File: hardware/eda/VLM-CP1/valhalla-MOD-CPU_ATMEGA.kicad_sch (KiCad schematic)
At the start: 16 parts, among them J1 ICSP, J2 BUS, U1 ATmega328PB-A, Y1 7.3728 MHz

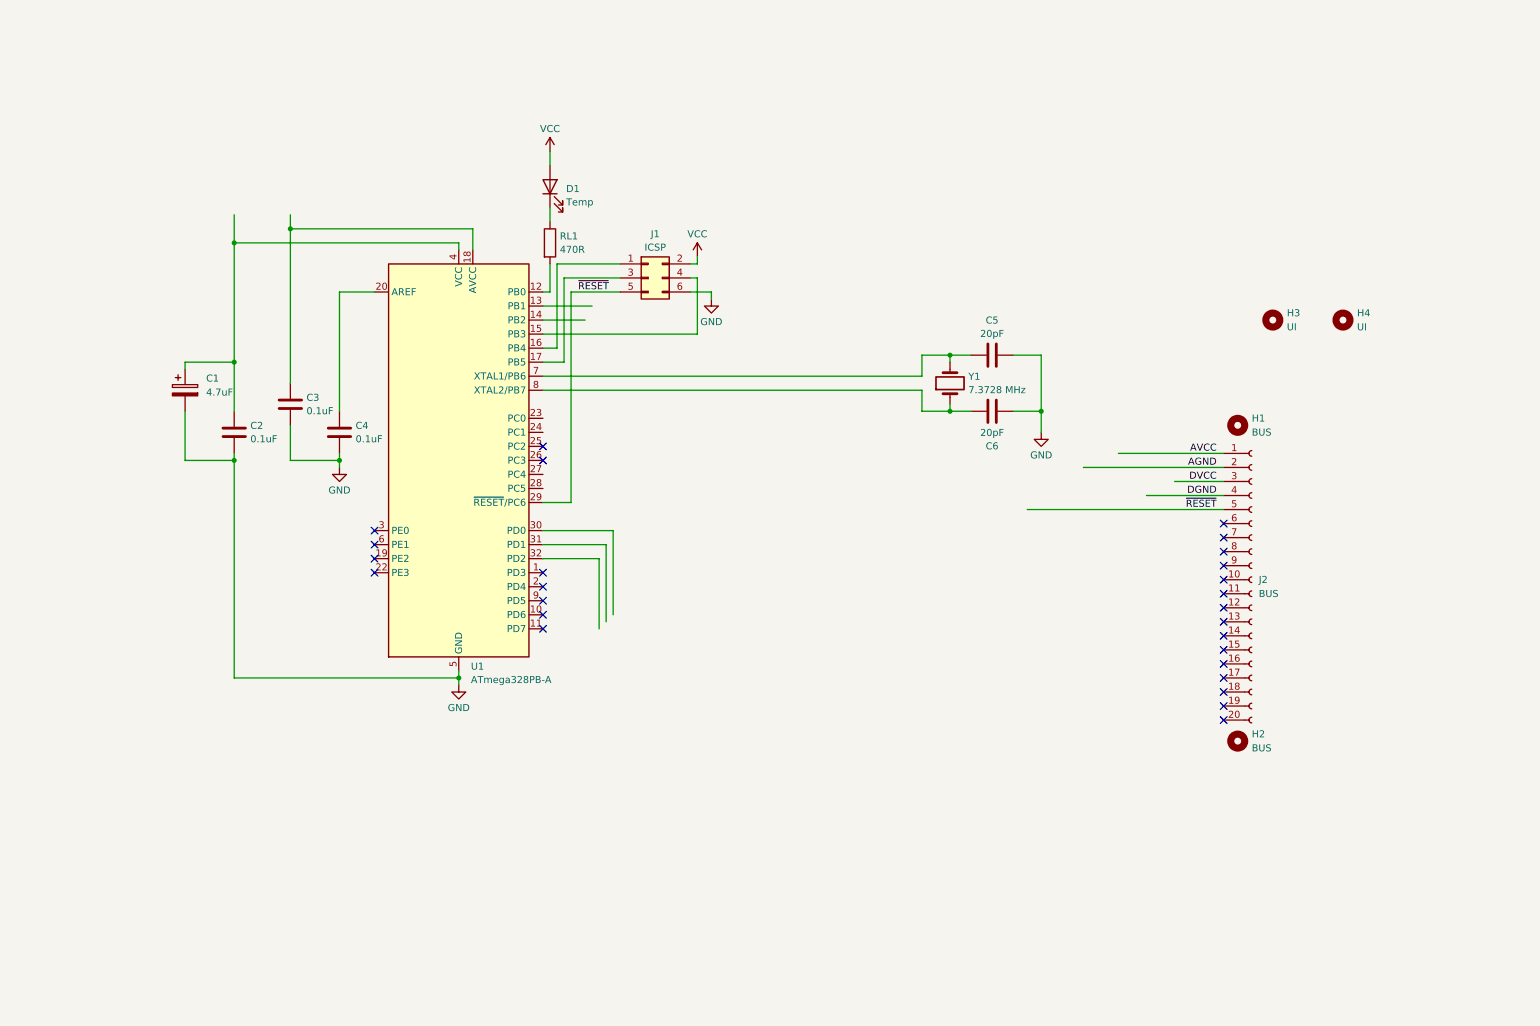
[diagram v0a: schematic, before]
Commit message: UPDATE: progress with the CPU(ATMega328) module
 - ATMega328 boilerplate done, BUS and UI done, GPIO done
 - LED UI in progress.
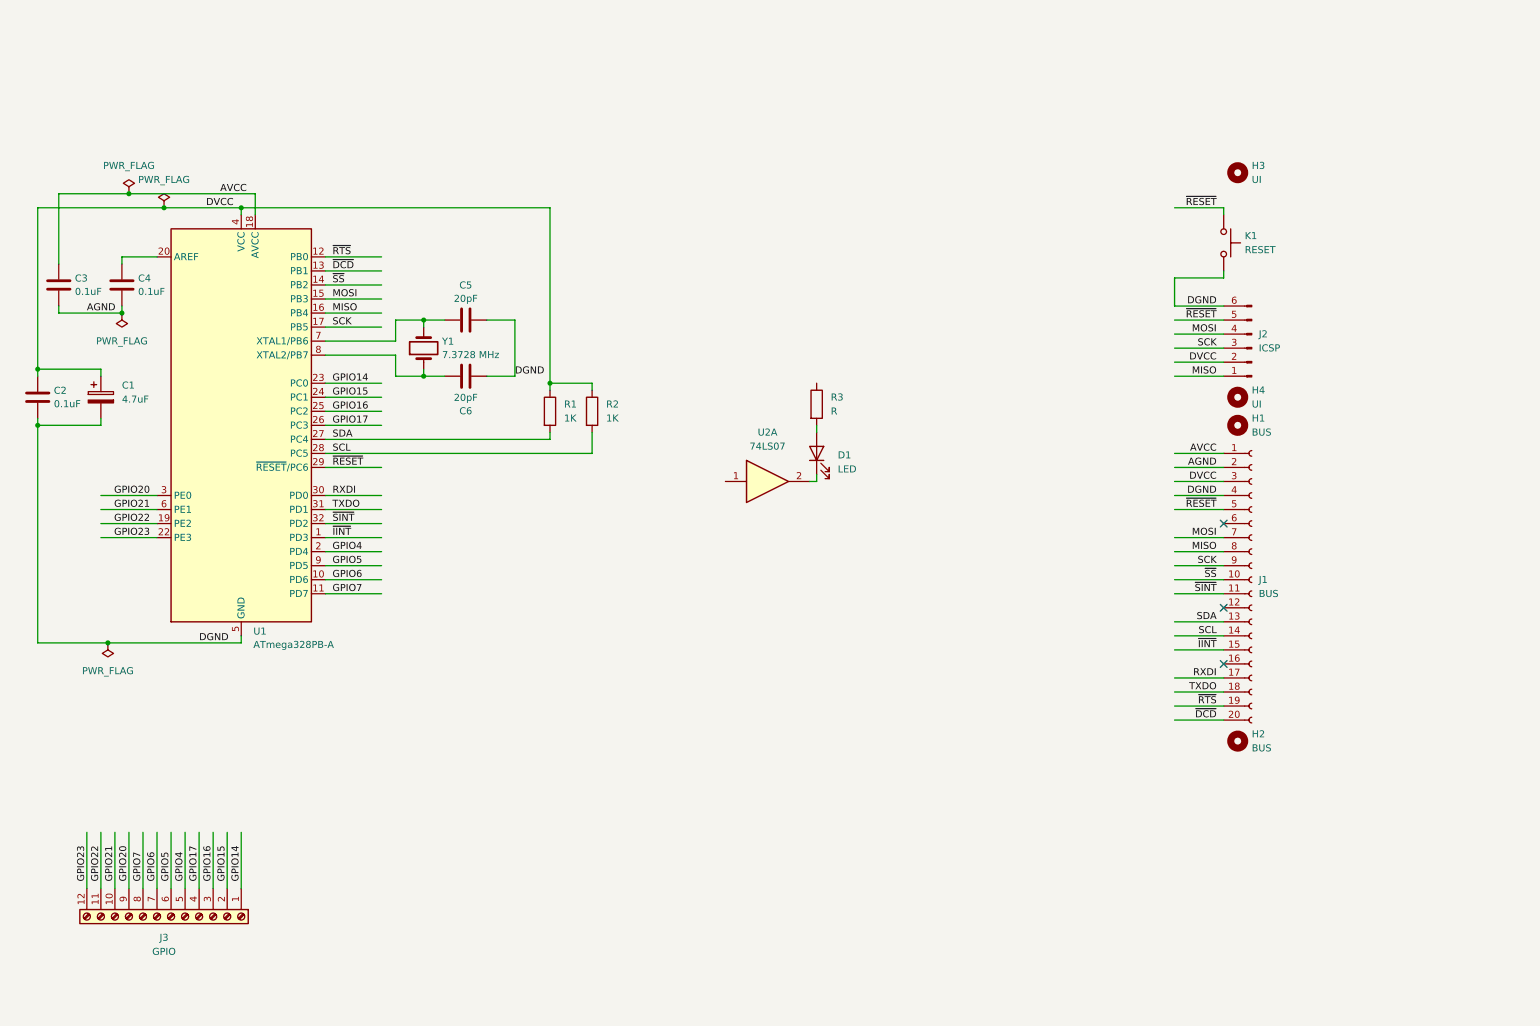
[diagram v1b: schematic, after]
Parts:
- removed J1: ICSP, Connector_IDC:IDC-Header_2x03_P2.54mm_Vertical, symbol Connector_Generic:Conn_02x03_Odd_Even
- removed RL1: 470R, Resistor_SMD:R_1206_3216Metric, symbol Device:R
- added J2: ICSP, Connector_IDC:IDC-Header_2x03_P2.54mm_Horizontal, symbol Connector:Conn_01x06_Pin
- added J3: GPIO, symbol Connector:Screw_Terminal_01x12
- added K1: RESET, symbol Switch:SW_Push
- added R1, R2: 1K, symbol Device:R
- added R3: R, symbol Device:R
- added U2: 74LS07, symbol 74xx:74LS07
- D1: value Temp -> LED; footprint LED_THT:LED_D5.0mm -> LED_THT:LED_D3.0mm_Horizontal_O1.27mm_Z2.0mm
- renumbered J2 to J1
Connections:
- net AGND: now also C3.2, C4.2
- net AVCC: now also C3.1, U1.18 (AVCC)
- net DGND: now also C1.2, C2.2, C5.2, C6.2, U1.21 (GND), U1.5 (GND), J2.6 (Pin_6), K1.2
- net DVCC: now also C1.1, C2.1, U1.4 (VCC), J2.2 (Pin_2), R1.1, R2.1
- net ~{RESET}: now also J2.5 (Pin_5), K1.1
- net at D1.1 (K): now also U2.2
- net ~{RTS}: now reaches U1.12 (PB0)
- net ~{RTS}: now also J1.19 (Pin_19)
- net MISO: now reaches U1.16 (PB4)
- net MISO: now also J1.8 (Pin_8), J2.1 (Pin_1)
- net SCK: now reaches U1.17 (PB5)
- net SCK: now also J1.9 (Pin_9), J2.3 (Pin_3)
- net MOSI: now reaches U1.15 (PB3)
- net MOSI: now also J1.7 (Pin_7), J2.4 (Pin_4)
- net ~{SS}: now reaches J1.10 (Pin_10)
- net ~{SS}: now also U1.14 (PB2)
- net ~{SINT}: now reaches J1.11 (Pin_11)
- net ~{SINT}: now also U1.32 (PD2)
- net SDA: now reaches J1.13 (Pin_13)
- net SDA: now also U1.27 (PC4), R1.2
- net SCL: now reaches J1.14 (Pin_14)
- net SCL: now also U1.28 (PC5), R2.2
- net ~{IINT}: now reaches J1.15 (Pin_15)
- net ~{IINT}: now also U1.1 (PD3)
- net RXDI: now reaches J1.17 (Pin_17)
- net RXDI: now also U1.30 (PD0)
- net TXDO: now reaches J1.18 (Pin_18)
- net TXDO: now also U1.31 (PD1)
- net ~{DCD}: now reaches J1.20 (Pin_20)
- net ~{DCD}: now also U1.13 (PB1)
- net GPIO6: now reaches U1.10 (PD6)
- net GPIO6: now also J3.7 (Pin_7)
- net GPIO7: now reaches U1.11 (PD7)
- net GPIO7: now also J3.8 (Pin_8)
- net GPIO22: now reaches U1.19 (PE2)
- net GPIO22: now also J3.11 (Pin_11)
- net GPIO4: now reaches U1.2 (PD4)
- net GPIO4: now also J3.5 (Pin_5)
- net GPIO23: now reaches U1.22 (PE3)
- net GPIO23: now also J3.12 (Pin_12)
- net GPIO14: now reaches U1.23 (PC0)
- net GPIO14: now also J3.1 (Pin_1)
- net GPIO15: now reaches U1.24 (PC1)
- net GPIO15: now also J3.2 (Pin_2)
- net GPIO16: now reaches U1.25 (PC2)
- net GPIO16: now also J3.3 (Pin_3)
- net GPIO17: now reaches U1.26 (PC3)
- net GPIO17: now also J3.4 (Pin_4)
- net GPIO20: now reaches U1.3 (PE0)
- net GPIO20: now also J3.9 (Pin_9)
- net GPIO21: now reaches U1.6 (PE1)
- net GPIO21: now also J3.10 (Pin_10)
- net GPIO5: now reaches U1.9 (PD5)
- net GPIO5: now also J3.6 (Pin_6)
- removed net GND: C1.2, C2.2, C3.2, C4.2, C5.2, C6.2, U1.21 (GND), U1.5 (GND)
- net VCC: no longer names the net of D1.2 (A)
- net VCC: now also R3.2
- no-connect marks 26 -> 3
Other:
- moved on the sheet: C1, C2, C3, C4, C5, C6, H3, H4, U1, Y1

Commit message: UPDATE: schematic complete of Valhalla-MOD CPU (ATMega) module
  - we still don't have a solution for powering the LEDs while obeying
    the design constraint that all modules must be agnostic to Vio
    inside [3.3V, 5V]
  - initial PCB component placement hints at 3" height for CPU (ATMega)
    module.
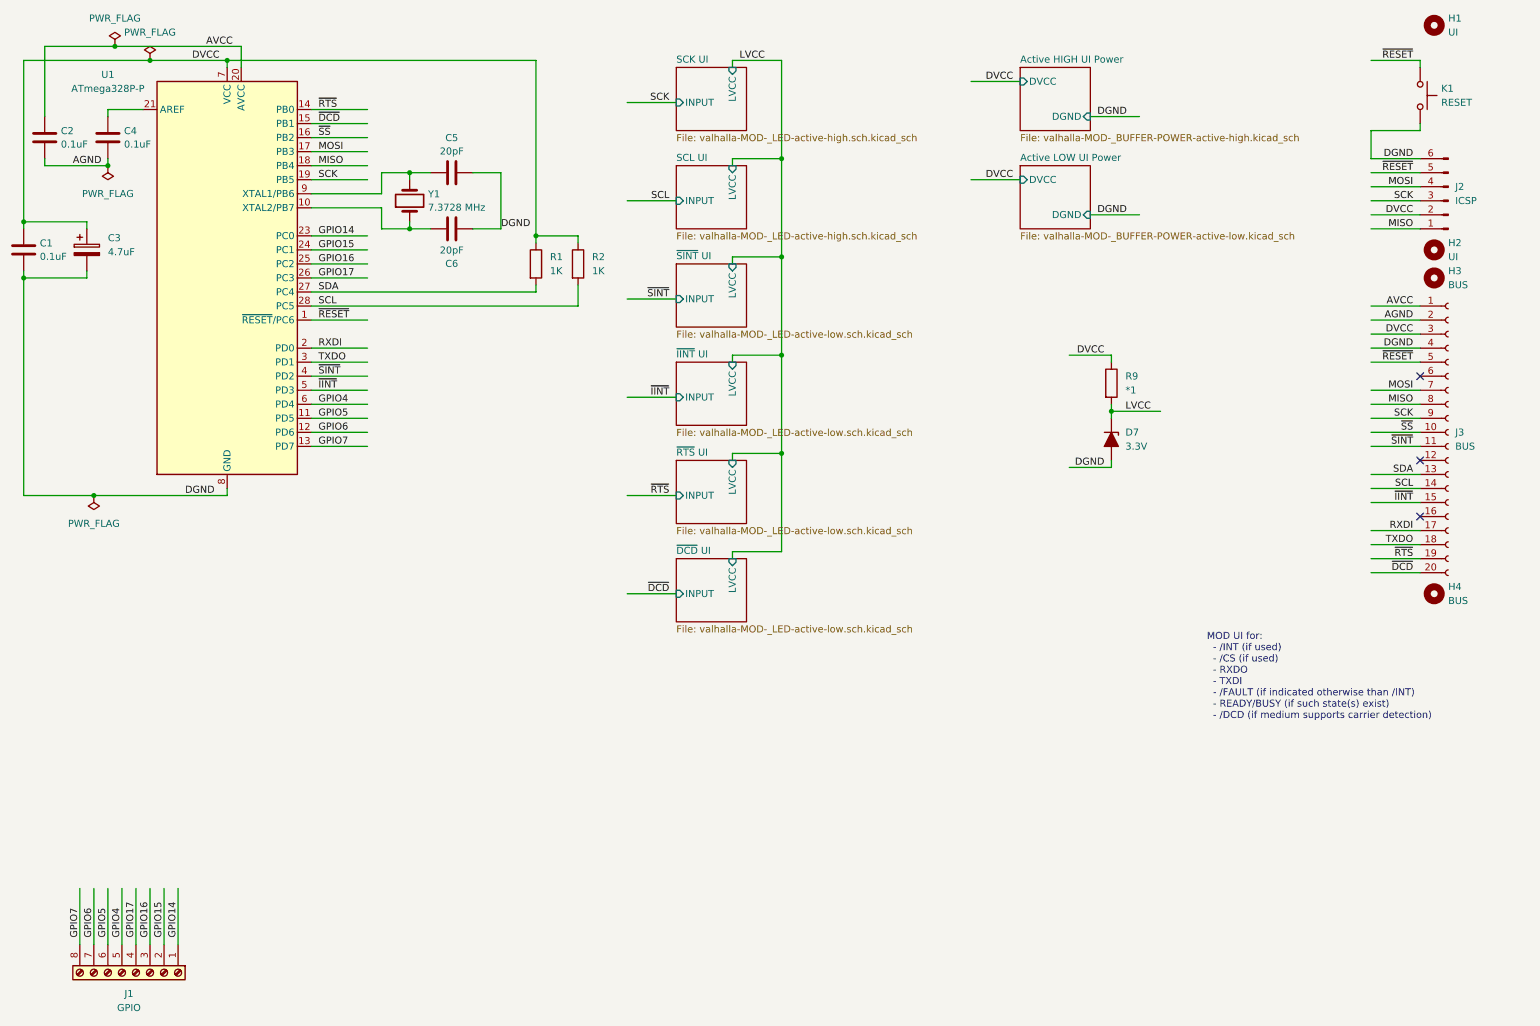
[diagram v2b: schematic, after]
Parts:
- removed D1: LED, LED_THT:LED_D3.0mm_Horizontal_O1.27mm_Z2.0mm, symbol Device:LED
- removed J3: GPIO, symbol Connector:Screw_Terminal_01x12
- removed R3: R, symbol Device:R
- removed U1: ATmega328PB-A, Package_QFP:TQFP-32_7x7mm_P0.8mm, symbol MCU_Microchip_ATmega:ATmega328PB-A
- removed U2: 74LS07, symbol 74xx:74LS07
- added D7: 3.3V, Diode_THT:D_DO-35_SOD27_P7.62mm_Horizontal, symbol Device:D_Zener_Filled
- added J1: GPIO, TerminalBlock_Phoenix:TerminalBlock_Phoenix_MPT-0,5-8-2.54_1x08_P2.54mm_Horizontal, symbol Connector:Screw_Terminal_01x08
- added R9: *1, Resistor_THT:R_Axial_DIN0309_L9.0mm_D3.2mm_P12.70mm_Horizontal, symbol Device:R
- added U1: ATmega328P-P, Package_DIP:DIP-28_W7.62mm, symbol MCU_Microchip_ATmega:ATmega328P-P
- C1: renamed from C2; footprint Capacitor_SMD:C_1206_3216Metric -> Capacitor_THT:C_Rect_L4.6mm_W2.0mm_P2.50mm_MKS02_FKP02
- C2: renamed from C3; footprint Capacitor_SMD:C_1206_3216Metric -> Capacitor_THT:C_Rect_L4.6mm_W2.0mm_P2.50mm_MKS02_FKP02
- C3: renamed from C1; footprint Capacitor_SMD:C_1206_3216Metric -> Capacitor_THT:CP_Radial_D5.0mm_P2.50mm
- C4: footprint Capacitor_SMD:C_1206_3216Metric -> Capacitor_THT:C_Rect_L4.6mm_W2.0mm_P2.50mm_MKS02_FKP02
- C5, C6: footprint Capacitor_SMD:C_1206_3216Metric -> Capacitor_THT:C_Disc_D5.0mm_W2.5mm_P5.00mm
- K1: footprint (none) -> Button_Switch_THT:SW_Tactile_SKHH_Angled
- R1, R2: footprint (none) -> Resistor_THT:R_Axial_DIN0309_L9.0mm_D3.2mm_P12.70mm_Horizontal
- Y1: footprint Crystal:Crystal_SMD_HC49-SD -> Crystal:Crystal_HC49-U_Horizontal
- renumbered H3 to H1, H4 to H2, H1 to H3, H2 to H4, J1 to J3
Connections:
- net AVCC: now also U1.20 (AVCC)
- net DGND: now also D7.2 (A), U1.22 (GND), U1.8 (GND)
- net DVCC: now also R9.1, U1.7 (VCC)
- net GPIO14: now also J1.1 (Pin_1), U1.23 (PC0)
- net GPIO15: now also J1.2 (Pin_2), U1.24 (PC1)
- net GPIO16: now also J1.3 (Pin_3), U1.25 (PC2)
- net GPIO17: now also J1.4 (Pin_4), U1.26 (PC3)
- net GPIO4: now also J1.5 (Pin_5), U1.6 (PD4)
- net GPIO5: now also J1.6 (Pin_6), U1.11 (PD5)
- net GPIO6: now also J1.7 (Pin_7), U1.12 (PD6)
- net GPIO7: now also J1.8 (Pin_8), U1.13 (PD7)
- net MISO: now also U1.18 (PB4)
- net MOSI: now also U1.17 (PB3)
- net RXDI: now also U1.2 (PD0)
- net SCK: now also U1.19 (PB5)
- net SCL: now also U1.28 (PC5)
- net SDA: now also U1.27 (PC4)
- net TXDO: now also U1.3 (PD1)
- net ~{DCD}: now also U1.15 (PB1)
- net ~{IINT}: now also U1.5 (PD3)
- net ~{RESET}: now also U1.1 (~{RESET}/PC6)
- net ~{RTS}: now also U1.14 (PB0)
- net ~{SINT}: now also U1.4 (PD2)
- net ~{SS}: now also U1.16 (PB2)
- net at C6.1, Y1.1: now also U1.10 (XTAL2/PB7)
- net at C4.1: now also U1.21 (AREF)
- net at C5.1, Y1.2: now also U1.9 (XTAL1/PB6)
- new net LVCC: D7.1 (K), R9.2
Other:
- added sheet Active HIGH UI Power (valhalla-MOD-_BUFFER-POWER-active-high.kicad_sch)
- added sheet Active LOW UI Power (valhalla-MOD-_BUFFER-POWER-active-low.kicad_sch)
- added sheet SCK UI (valhalla-MOD-_LED-active-high.sch.kicad_sch)
- added sheet SCL UI (valhalla-MOD-_LED-active-high.sch.kicad_sch)
- added sheet ~{DCD} UI (valhalla-MOD-_LED-active-low.sch.kicad_sch)
- added sheet ~{IINT} UI (valhalla-MOD-_LED-active-low.sch.kicad_sch)
- added sheet ~{RTS} UI (valhalla-MOD-_LED-active-low.sch.kicad_sch)
- added sheet ~{SINT} UI (valhalla-MOD-_LED-active-low.sch.kicad_sch)
- note added: "MOD UI for: - /INT (if used) - /CS (if used) - RXDO - TXDI - /FAULT (if indicated otherwise than /INT) - READY/BUSY (if such state(s) exist) - /DCD (if medium supports carrier detection)"
- moved on the sheet: C1, C2, C3, C4, C5, C6, H1, H2, H3, H4, J2, J3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

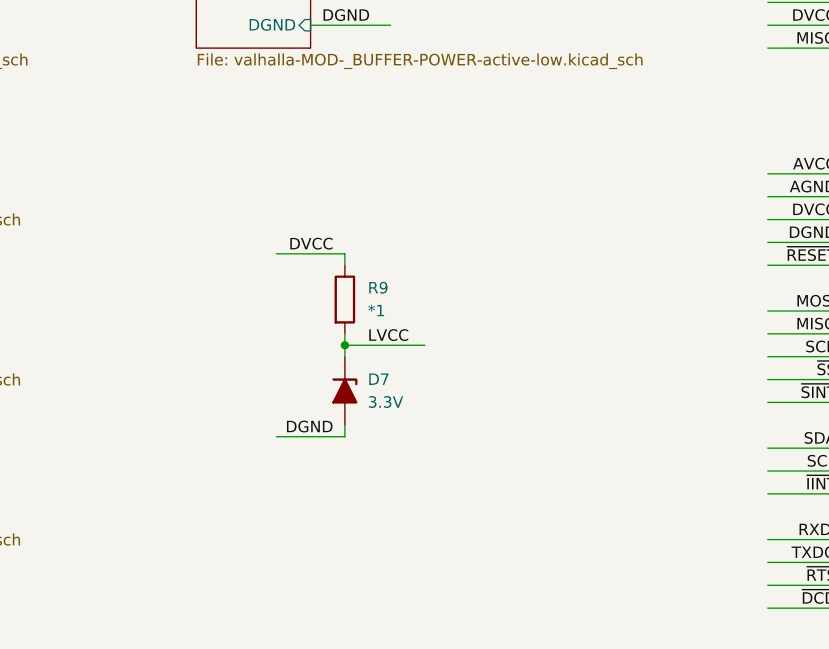
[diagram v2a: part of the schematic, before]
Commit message: UPDATE: formal dimensions for Valhalla MOD and progrss on CPU
 - added formal dimensions to the Valhalla MOD PSU PCB, to serve as a
   future template and as documentation
 - changed Zener/Schottky symbols to filled variant on same module,
   as customary in the EU
 - solved the Vio independence issue for the UI LEDs on the CPU module
   with a switchable regulator
 - finalized canonical dimensions of the CPU module and placed UI
   LEDs in two rows.
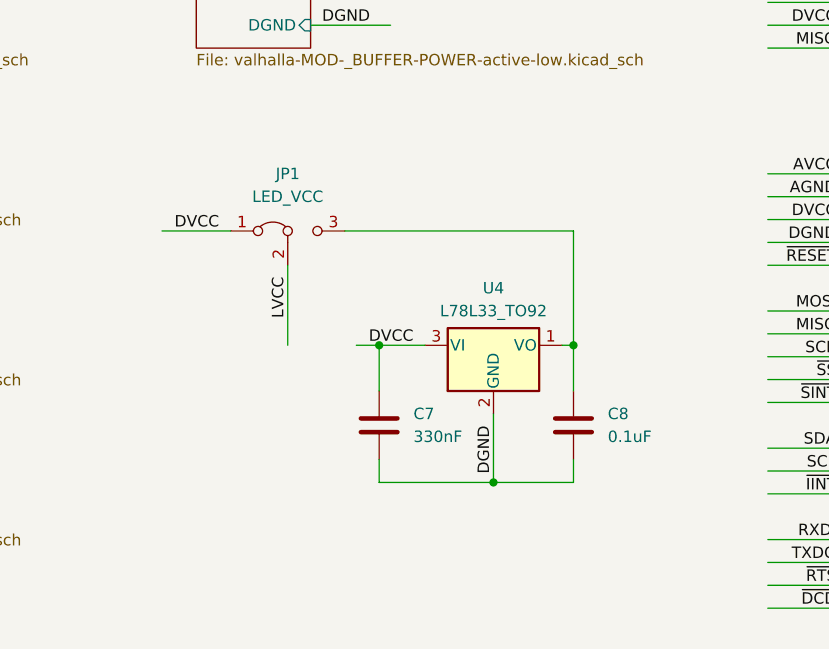
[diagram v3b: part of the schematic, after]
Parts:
- removed D7: 3.3V, Diode_THT:D_DO-35_SOD27_P7.62mm_Horizontal, symbol Device:D_Zener_Filled
- removed R9: *1, Resistor_THT:R_Axial_DIN0309_L9.0mm_D3.2mm_P12.70mm_Horizontal, symbol Device:R
- added C7: 330nF, symbol Device:C
- added C8: 0.1uF, symbol Device:C
- added JP1: LED_VCC, Connector_PinHeader_2.54mm:PinHeader_1x03_P2.54mm_Vertical, symbol Jumper:Jumper_3_Bridged12
- added U4: L78L33_TO92, Package_TO_SOT_THT:TO-92_Inline, symbol Regulator_Linear:L78L33_TO92
- R1, R2: footprint Resistor_THT:R_Axial_DIN0309_L9.0mm_D3.2mm_P12.70mm_Horizontal -> Resistor_THT:R_Axial_DIN0207_L6.3mm_D2.5mm_P10.16mm_Horizontal
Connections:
- net DGND: now also C7.2, C8.2, U4.2 (GND)
- net DVCC: now also C7.1, JP1.1 (A), U4.3 (VI)
- net LVCC: now also JP1.2 (C)
- new net: C8.1, JP1.3 (B), U4.1 (VO)
